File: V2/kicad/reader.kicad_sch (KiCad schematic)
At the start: 88 parts, among them SW1 SW_Rezistance, SW2 SW_src, U1 STM32H523CET6, U2 MAX98357AETE+T, U3 MLD-TF PUSH-H18, U4 TCAN1057AVDRQ1, U5 ESD2CAN24-ES, U6 RJ-064-1, U7 MCP16301Hx-xCH, Y1 16MHz

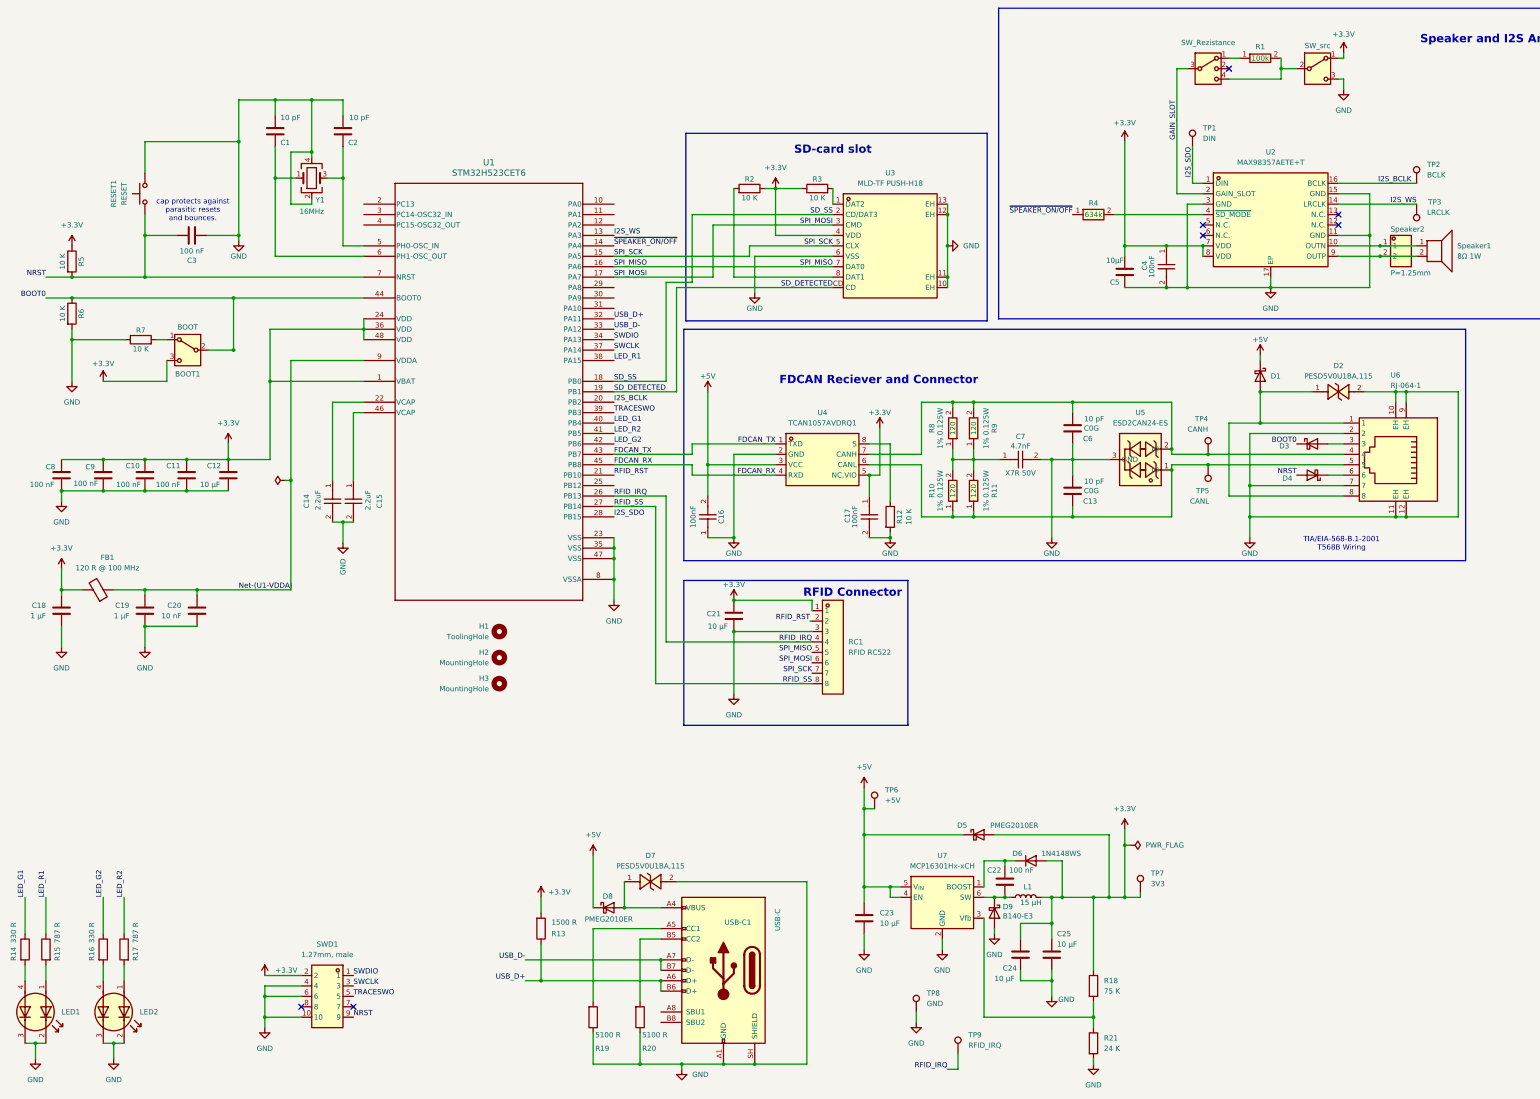
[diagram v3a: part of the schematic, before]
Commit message: changed size of pcb paper to A5 added labels and groups to schematic
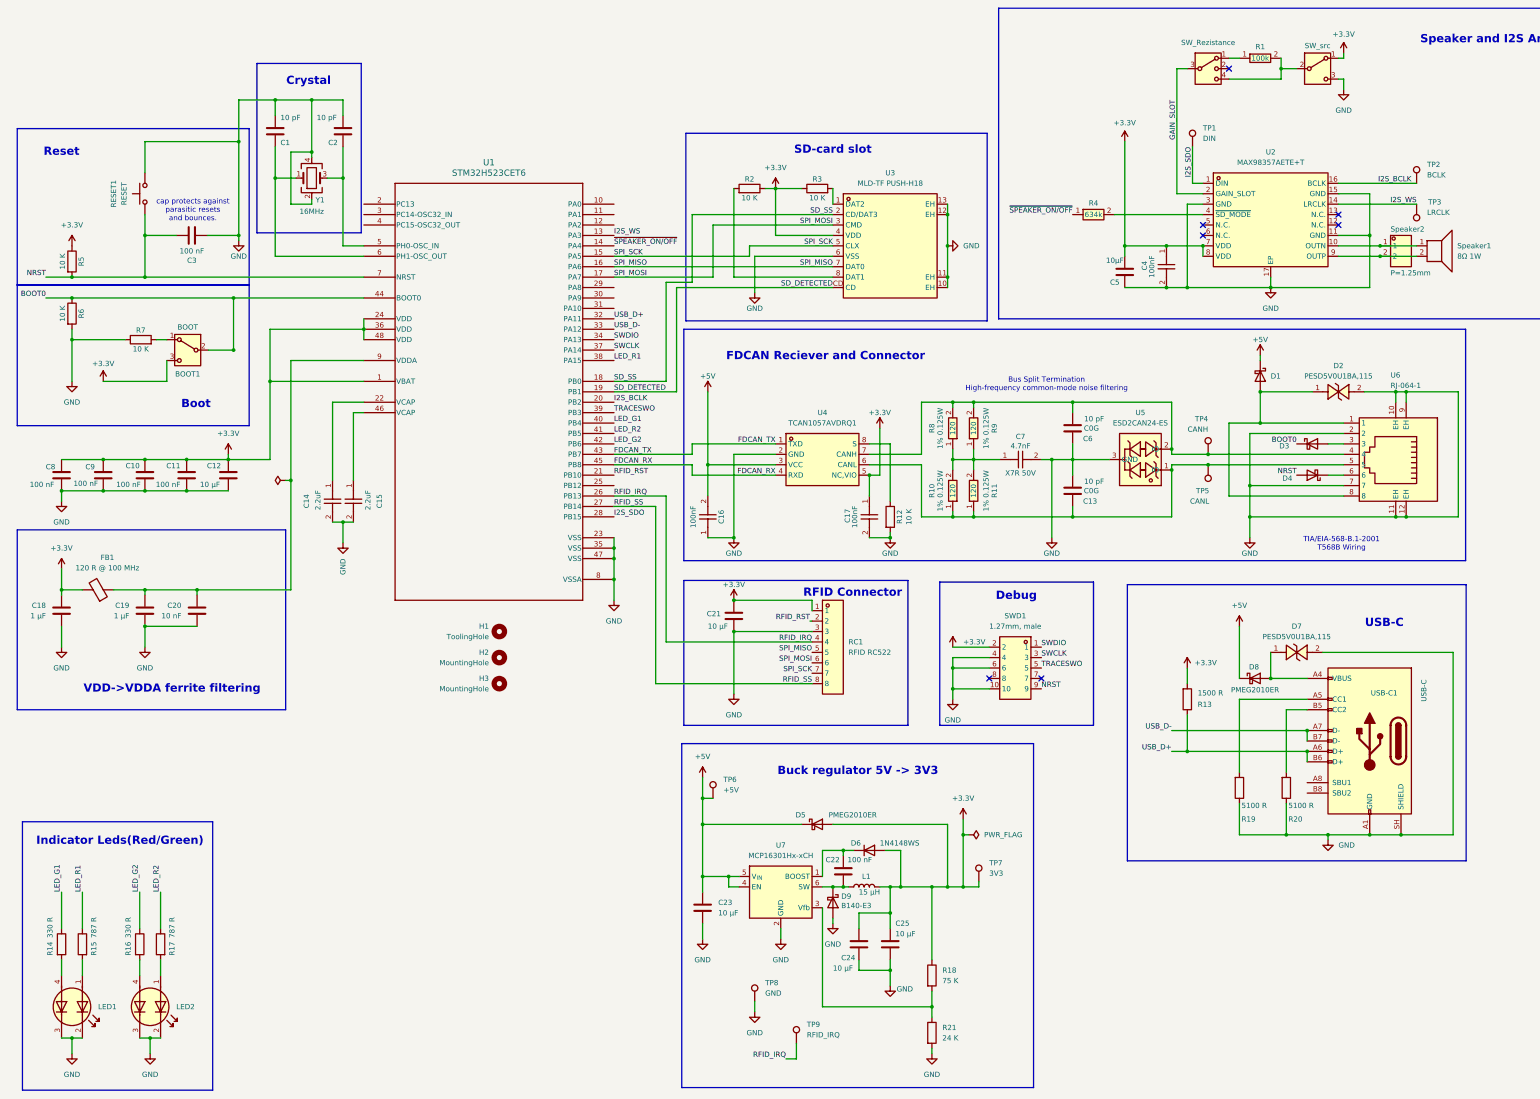
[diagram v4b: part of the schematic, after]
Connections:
- net Net-(U1-VDDA): no longer names the net of C19.1, C20.1, FB1.1, U1.9 (VDDA)
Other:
- note added: "Boot"
- note added: "Buck regulator 5V -> 3V3"
- note added: "Bus Split Termination High-frequency common-mode noise filtering"
- note added: "Crystal"
- note added: "Debug"
- note added: "Indicator Leds(Red/Green)"
- note added: "Reset"
- note added: "USB-C"
- note added: "VDD->VDDA ferrite filtering"
- moved on the sheet: C2, C22, C23, C24, C25, D5, D6, D7, D8, D9, L1, LED1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

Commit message: .
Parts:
- H1, H2, H3: now in the parts list
- R10, R11, R8, R9: LCSC Part C49254430 -> C17437

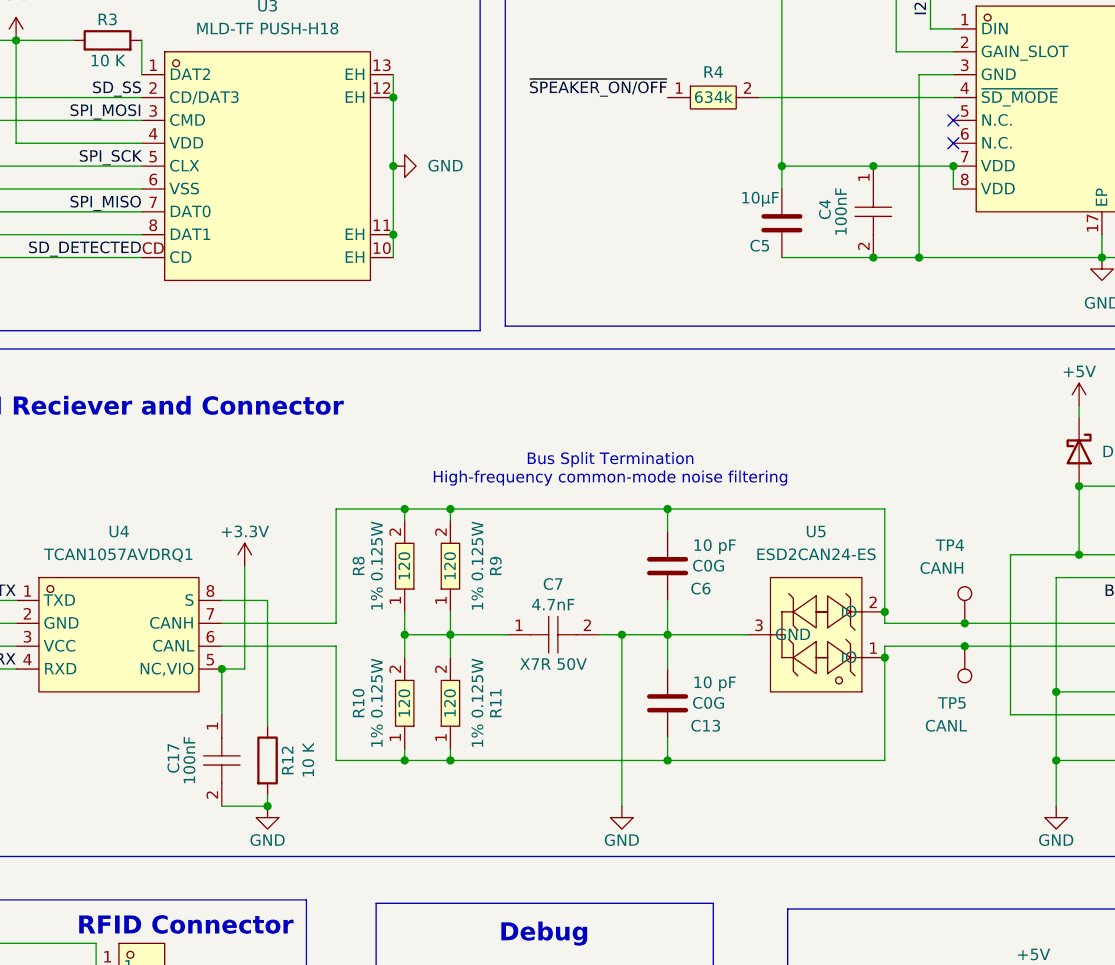
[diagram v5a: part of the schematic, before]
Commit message: changed few components because of availability. moved thesis into this repository.
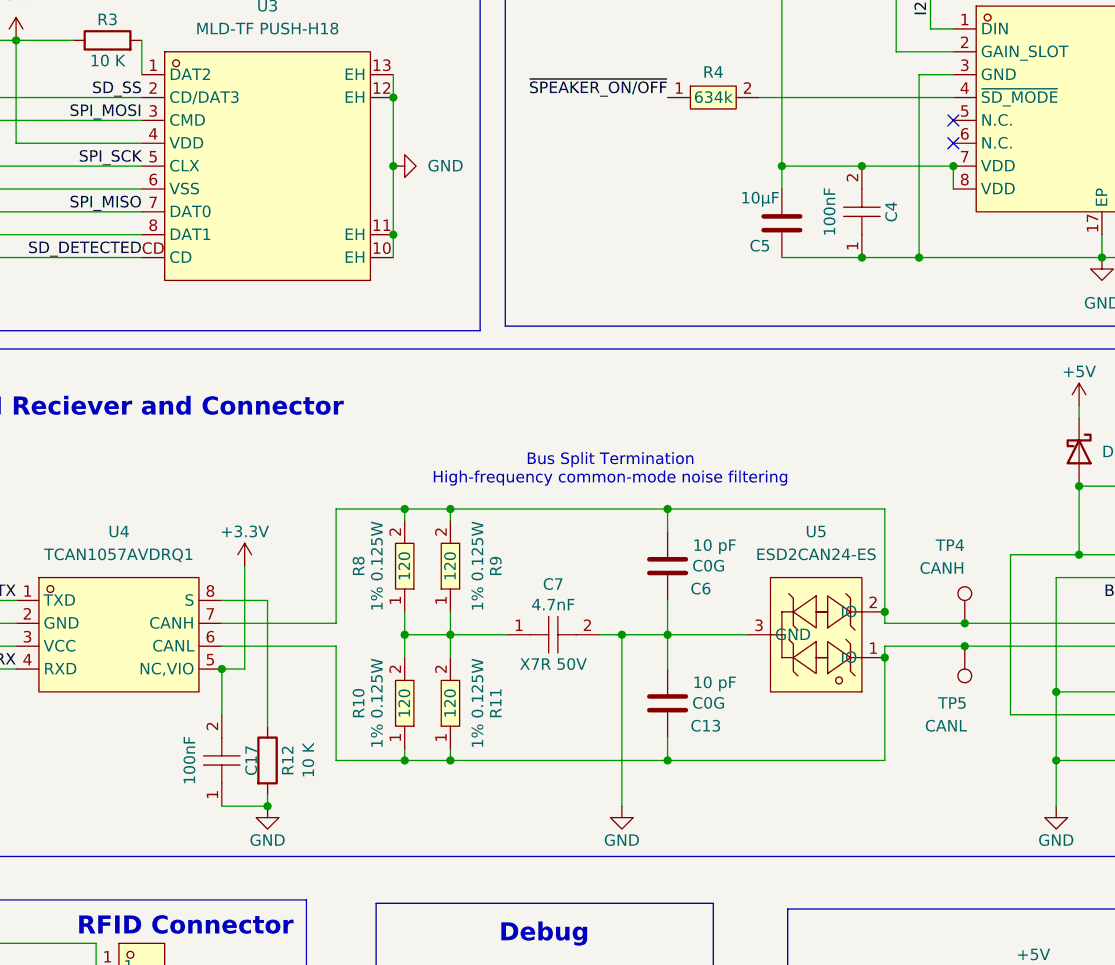
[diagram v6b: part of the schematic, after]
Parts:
- C16, C17, C4: value CL10B104KC8NNNC -> CC0603KRX7R9BB104; LCSC Part C15725 -> C14663; MPN CL10B104KC8NNNC -> CC0603KRX7R9BB104; Manufacturer SAMSUNG(三星) -> YAGEO
- R1: value RC1206JR-07100KL -> 0603WAF1003T5E; footprint easyeda2kicad:R1206 -> easyeda2kicad:R0603; LCSC Part C136470 -> C25803; MPN RC1206JR-07100KL -> 0603WAF1003T5E; Manufacturer YAGEO(国巨) -> UNI-ROYAL(厚声)
- R15, R17: JLCPCB https://www.lcsc.com/product-detail/C270582.html -> https://www.lcsc.com/product-detail/C4109.html; LCSC C270582 -> C4109
- R4: value RC0805FR-07634KL -> 0805W8F1501T5E; LCSC Part C483209 -> C4310; MPN RC0805FR-07634KL -> 0805W8F1501T5E; Manufacturer YAGEO(国巨) -> UNI-ROYAL(Uniroyal Elec)
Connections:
- net +3.3V: now also C17.2, C4.2; no longer C17.1, C4.1
- net GND: now also C17.1, C4.1; no longer C17.2, C4.2
